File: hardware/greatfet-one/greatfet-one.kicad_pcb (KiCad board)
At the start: 4 copper layers, 70.6 x 53.3 mm, 97 parts, among them J1 NEIGHBOR1, J2 NEIGHBOR2, J3 USB-MICRO-B-SHIELDED, J4 USB-MICRO-B-SHIELDED, J5 JTAG, J7 BONUS_ROW, SW1 DFU, SW2 RESET, U1 LPC4330FBD144, U2 W25Q16DV, U3 AP7333, U4 IP4220CZ6, U5 AP2553W6-7, X1 MCU_XTAL, X2 RTC_XTAL

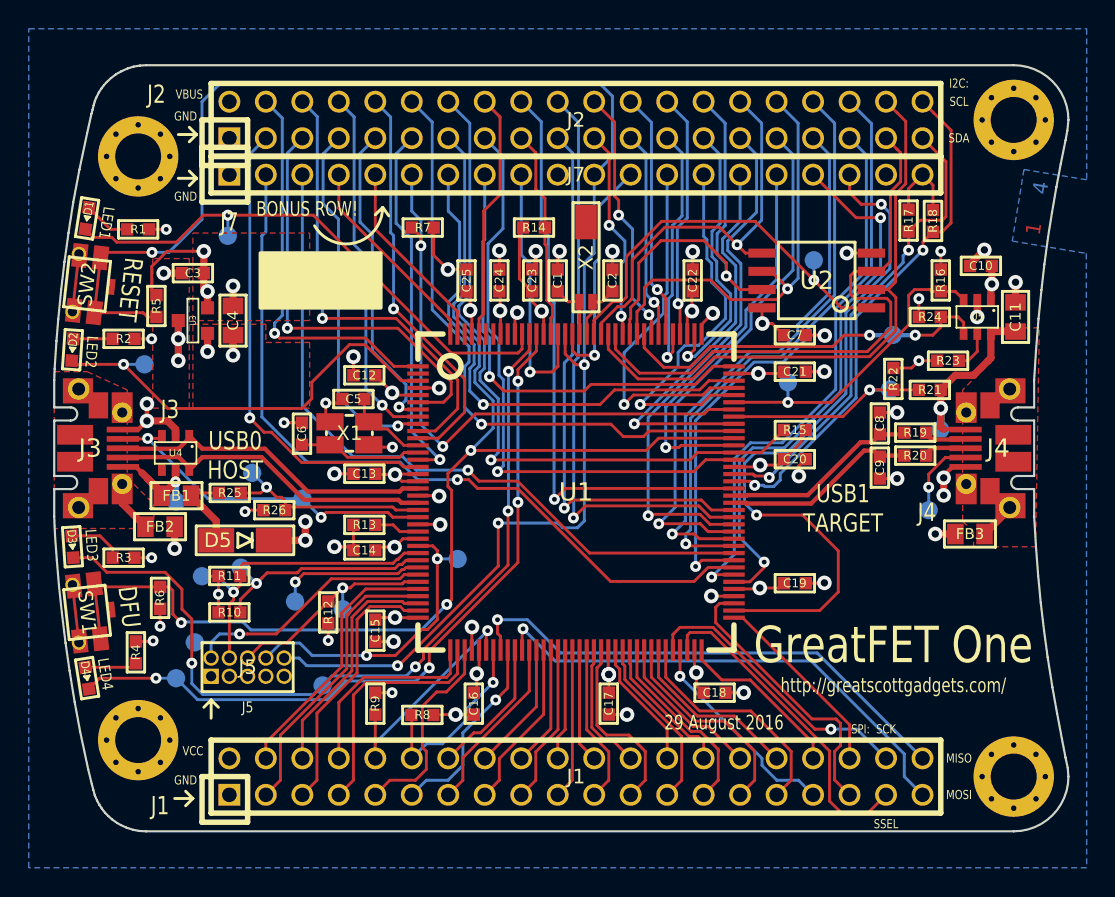
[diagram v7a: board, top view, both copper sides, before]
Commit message: GreatFET One: J6 POWER header on bottom, can be used with single row header on edge, could be useful for non-USB applications of U5 power switch
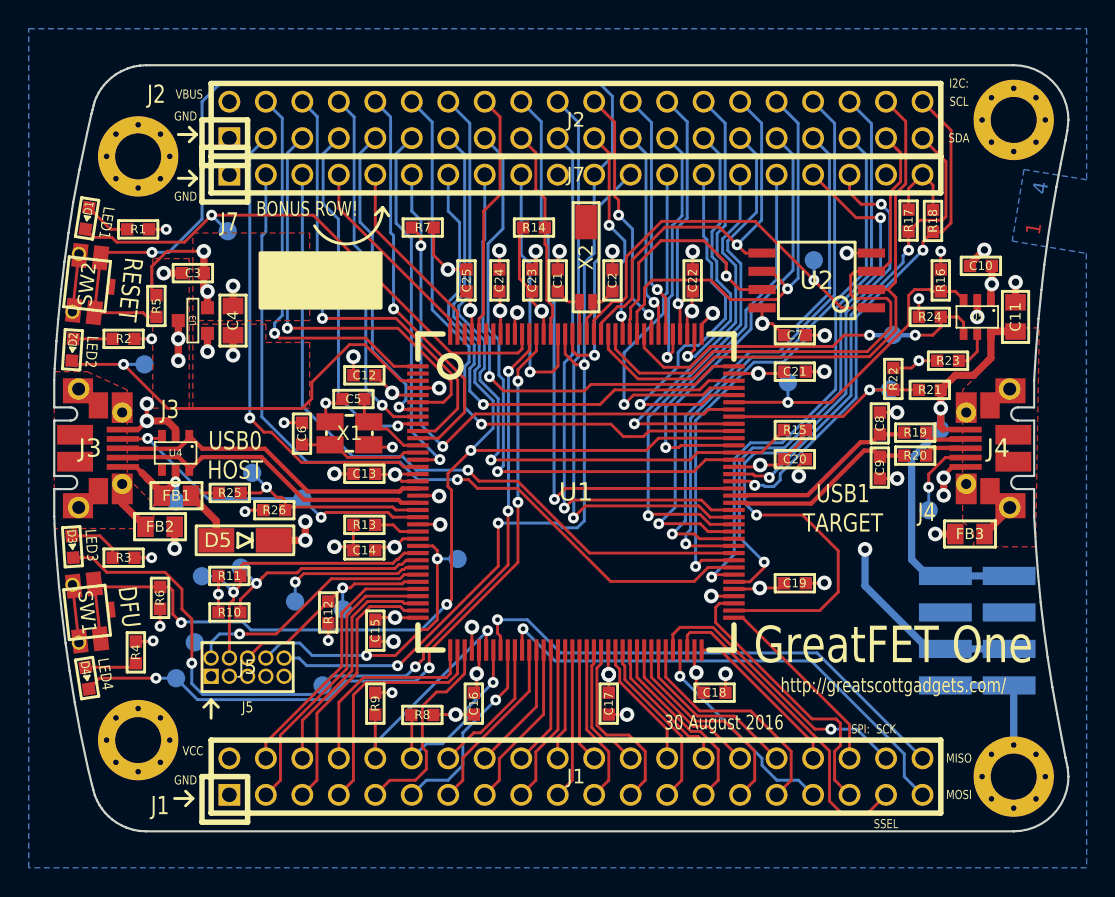
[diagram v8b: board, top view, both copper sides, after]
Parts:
- added J6: POWER, gsg-modules:HEADER-SMT-2x4, B.Cu at (170.2, 110.5)
- moved TP3 0.32 mm to (118.0, 82.7)
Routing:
- net /USB1_VBUS: track 13.8 -> 30.9 mm
- net VCC: track 88.9 -> 103.3 mm, vias 26 -> 27
- net GND: track 82.5 -> 93.5 mm
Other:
- board text added: "30 August 2016"
- board text removed: "29 August 2016"
